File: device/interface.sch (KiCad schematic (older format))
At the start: 30 parts, among them IC1 ATTINY2313-S, J1 Screw_Terminal_1x02, J2 Screw_Terminal_01x02, P1 CONN_01X06, P2 CONN_02X03, P3 CONN_01X04, U1 L7805, U2 MAX483E, Y1 16MHz

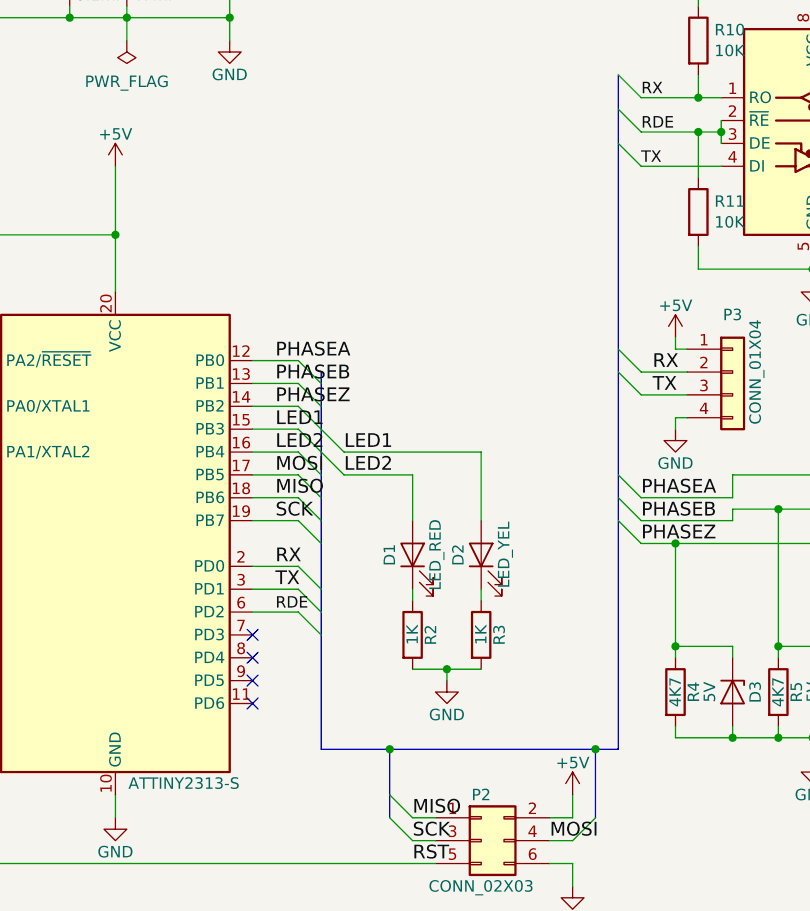
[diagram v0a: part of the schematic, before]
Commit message: added address switch
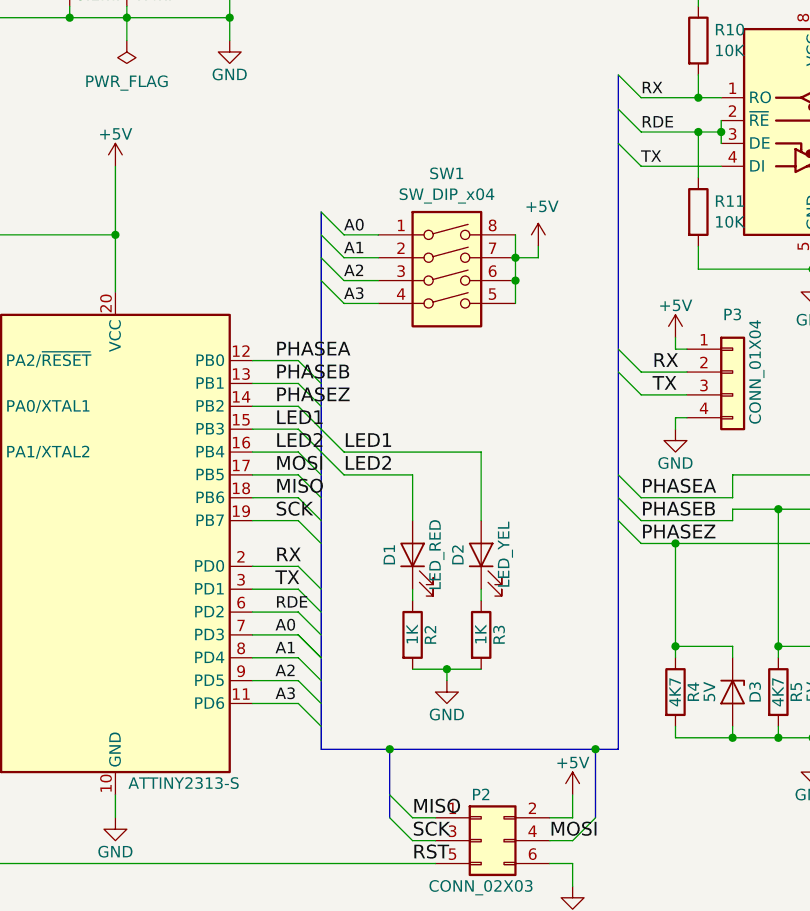
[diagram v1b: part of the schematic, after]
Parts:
- added SW1: SW_DIP_x04, Button_Switch_THT:SW_DIP_SPSTx04_Slide_9.78x12.34mm_W7.62mm_P2.54mm, symbol Switch:SW_DIP_x04
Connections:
- net +5V: now also SW1.5, SW1.6, SW1.7, SW1.8
- net A3: now reaches IC1.11 (PD6)
- net A3: now also SW1.4
- net A0: now reaches IC1.7 (PD3)
- net A0: now also SW1.1
- net A1: now reaches IC1.8 (PD4)
- net A1: now also SW1.2
- net A2: now reaches IC1.9 (PD5)
- net A2: now also SW1.3
- no-connect marks 4 -> 0
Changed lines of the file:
@@
 EESchema Schematic File Version 4
+LIBS:interface-cache
 EELAYER 26 0
 EELAYER END
@@
 	1    0    0    -1
 $EndComp
-NoConn ~ 6950 4100
-NoConn ~ 6950 4200
-NoConn ~ 6950 4300
-NoConn ~ 6950 4400
 $Comp
 L power:PWR_FLAG #FLG014
@@
 Wire Wire Line
 	9800 2050 10000 2050
+$Comp
+L Switch:SW_DIP_x04 SW1
+U 1 1 5D7BE9E3
+P 7800 2550
+F 0 "SW1" H 7800 3017 50  0000 C CNN
+F 1 "SW_DIP_x04" H 7800 2926 50  0000 C CNN
+F 2 "Button_Switch_THT:SW_DIP_SPSTx04_Slide_9.78x12.34mm_W7.62mm_P2.54mm" H 7800 2550 50  0001 C CNN
+F 3 "" H 7800 2550 50  0001 C CNN
+	1    7800 2550
+	1    0    0    -1
+$EndComp
+Wire Wire Line
+	8100 2350 8100 2450
+Wire Wire Line
+	8100 2550 8100 2450
+Connection ~ 8100 2450
+Wire Wire Line
+	8100 2650 8100 2550
+Connection ~ 8100 2550
+$Comp
+L power:+5V #PWR0103
+U 1 1 5D7CF99B
+P 8200 2400
+F 0 "#PWR0103" H 8200 2250 50  0001 C CNN
+F 1 "+5V" H 8215 2573 50  0000 C CNN
+F 2 "" H 8200 2400 50  0001 C CNN
+F 3 "" H 8200 2400 50  0001 C CNN
+	1    8200 2400
+	1    0    0    -1
+$EndComp
+Wire Wire Line
+	8200 2400 8200 2450
+Wire Wire Line
+	8200 2450 8100 2450
+Entry Wire Line
+	7250 2250 7350 2350
+Entry Wire Line
+	7250 2350 7350 2450
+Entry Wire Line
+	7250 2450 7350 2550
+Entry Wire Line
+	7250 2550 7350 2650
+Wire Wire Line
+	7500 2350 7350 2350
+Wire Wire Line
+	7500 2450 7350 2450
+Wire Wire Line
+	7500 2550 7350 2550
+Wire Wire Line
+	7500 2650 7350 2650
+Text Label 7350 2350 0    50   ~ 0
+A0
+Text Label 7350 2450 0    50   ~ 0
+A1
+Text Label 7350 2550 0    50   ~ 0
+A2
+Text Label 7350 2650 0    50   ~ 0
+A3
+Entry Wire Line
+	7150 4100 7250 4200
+Entry Wire Line
+	7150 4200 7250 4300
+Entry Wire Line
+	7150 4300 7250 4400
+Entry Wire Line
+	7150 4400 7250 4500
+Entry Wire Line
+	7150 4100 7250 4200
+Wire Wire Line
+	7150 4100 6950 4100
+Wire Wire Line
+	7150 4200 6950 4200
+Wire Wire Line
+	7150 4300 6950 4300
+Wire Wire Line
+	7150 4400 6950 4400
 Wire Bus Line
 	7550 4600 7550 4900
@@
 	8550 1650 8550 4600
 Wire Bus Line
-	7250 2950 7250 4600
+	7250 2250 7250 4600
+Text Label 7050 4100 0    50   ~ 0
+A0
+Text Label 7050 4200 0    50   ~ 0
+A1
+Text Label 7050 4300 0    50   ~ 0
+A2
+Text Label 7050 4400 0    50   ~ 0
+A3
 $EndSCHEMATC

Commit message: added address switch
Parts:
- SW1: value SW_DIP_x04 -> ADDRESS_SW
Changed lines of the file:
@@
 P 7800 2550
 F 0 "SW1" H 7800 3017 50  0000 C CNN
-F 1 "SW_DIP_x04" H 7800 2926 50  0000 C CNN
+F 1 "ADDRESS_SW" H 7800 2926 50  0000 C CNN
 F 2 "Button_Switch_THT:SW_DIP_SPSTx04_Slide_9.78x12.34mm_W7.62mm_P2.54mm" H 7800 2550 50  0001 C CNN
 F 3 "" H 7800 2550 50  0001 C CNN

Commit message: pcb update
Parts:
- added C5: 470mF, Capacitor_SMD:C_Elec_6.3x7.7, symbol Device:CP
- added C6: 0,1mF, Capacitor_SMD:C_0805_2012Metric, symbol Device:C
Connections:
- net +5V: now also C5.1, C6.1
- net GND: now also C5.2, C6.2
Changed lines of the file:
@@
 L power:+5V #PWR06
 U 1 1 5D7AEF69
-P 7300 950
-F 0 "#PWR06" H 7300 800 50  0001 C CNN
-F 1 "+5V" H 7300 1090 50  0000 C CNN
-F 2 "" H 7300 950 50  0000 C CNN
-F 3 "" H 7300 950 50  0000 C CNN
-	1    7300 950
+P 7750 950
+F 0 "#PWR06" H 7750 800 50  0001 C CNN
+F 1 "+5V" H 7750 1090 50  0000 C CNN
+F 2 "" H 7750 950 50  0000 C CNN
+F 3 "" H 7750 950 50  0000 C CNN
+	1    7750 950
 	1    0    0    -1
 $EndComp
@@
 Connection ~ 6150 1400
 Wire Wire Line
-	7300 1000 7300 950
+	7750 1000 7750 950
 Wire Bus Line
 	8450 4600 8450 4900
@@
 	6400 1000 6550 1000
 Wire Wire Line
-	7150 1000 7300 1000
+	7150 1000 7250 1000
 Wire Wire Line
 	6350 4800 6350 4900
@@
 Wire Wire Line
 	7150 4400 6950 4400
-Wire Bus Line
-	7550 4600 7550 4900
-Wire Bus Line
-	8550 1650 8550 4600
-Wire Bus Line
-	7250 2250 7250 4600
 Text Label 7050 4100 0    50   ~ 0
 A0
@@
 Text Label 7050 4400 0    50   ~ 0
 A3
+$Comp
+L Device:CP C5
+U 1 1 5D7F3934
+P 7250 1200
+F 0 "C5" H 7300 1300 50  0000 L CNN
+F 1 "470mF" H 7250 1100 50  0000 L CNN
+F 2 "Capacitor_SMD:C_Elec_6.3x7.7" H 7288 1050 50  0001 C CNN
+F 3 "~" H 7250 1200 50  0001 C CNN
+	1    7250 1200
+	1    0    0    -1
+$EndComp
+$Comp
+L Device:C C6
+U 1 1 5D7F3A01
+P 7550 1200
+F 0 "C6" H 7600 1300 50  0000 L CNN
+F 1 "0,1mF" H 7600 1100 50  0000 L CNN
+F 2 "Capacitor_SMD:C_0805_2012Metric" H 7588 1050 50  0001 C CNN
+F 3 "~" H 7550 1200 50  0001 C CNN
+	1    7550 1200
+	1    0    0    -1
+$EndComp
+Wire Wire Line
+	7250 1050 7250 1000
+Connection ~ 7250 1000
+Wire Wire Line
+	7250 1000 7550 1000
+Wire Wire Line
+	7550 1050 7550 1000
+Connection ~ 7550 1000
+Wire Wire Line
+	7550 1000 7750 1000
+Wire Wire Line
+	7250 1350 7250 1400
+Wire Wire Line
+	7250 1400 6850 1400
+Wire Wire Line
+	7550 1350 7550 1400
+Wire Wire Line
+	7550 1400 7250 1400
+Wire Bus Line
+	7550 4600 7550 4900
+Wire Bus Line
+	8550 1650 8550 4600
+Wire Bus Line
+	7250 2250 7250 4600
+Connection ~ 7250 1400
 $EndSCHEMATC

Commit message: uart pull uo
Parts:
- added R12: 10K, Resistor_SMD:R_0805_2012Metric, symbol Device:R
- C4: value 47mF -> 100mF
- C5: value 470mF -> 100mF
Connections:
- net +5V: now also R12.2
- net RX: now also R12.1
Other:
- moved on the sheet: P3
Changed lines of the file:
@@
 P 6400 1200
 F 0 "C4" H 6425 1300 50  0000 L CNN
-F 1 "47mF" H 6425 1100 50  0000 L CNN
+F 1 "100mF" H 6425 1100 50  0000 L CNN
 F 2 "Capacitor_SMD:CP_Elec_6.3x5.3" H 6438 1050 50  0001 C CNN
 F 3 "" H 6400 1200 50  0000 C CNN
@@
 L Connector_Generic:Conn_01x04 P3
 U 1 1 5D7B1EFF
-P 9050 2950
-F 0 "P3" H 9050 3200 50  0000 C CNN
-F 1 "CONN_01X04" V 9150 2950 50  0000 C CNN
-F 2 "Connector_JST:JST_XH_S4B-XH-A_1x04_P2.50mm_Horizontal" H 9050 2950 50  0001 C CNN
-F 3 "" H 9050 2950 50  0000 C CNN
-	1    9050 2950
+P 10600 2950
+F 0 "P3" H 10600 3200 50  0000 C CNN
+F 1 "CONN_01X04" V 10700 2950 50  0000 C CNN
+F 2 "Connector_JST:JST_XH_S4B-XH-A_1x04_P2.50mm_Horizontal" H 10600 2950 50  0001 C CNN
+F 3 "" H 10600 2950 50  0000 C CNN
+	1    10600 2950
 	1    0    0    -1
 $EndComp
@@
 	8800 2800 8800 2850
 Wire Wire Line
-	8800 2850 8850 2850
-Wire Wire Line
-	8850 3150 8800 3150
+	8800 2850 10200 2850
+Wire Wire Line
+	10400 3150 8800 3150
 Wire Wire Line
 	8800 3150 8800 3200
 Wire Wire Line
-	8650 3050 8850 3050
-Wire Wire Line
-	8850 2950 8650 2950
+	8650 3050 10400 3050
+Wire Wire Line
+	10400 2950 10100 2950
 Connection ~ 8800 3700
 Wire Wire Line
@@
 P 7250 1200
 F 0 "C5" H 7300 1300 50  0000 L CNN
-F 1 "470mF" H 7250 1100 50  0000 L CNN
+F 1 "100mF" H 7250 1100 50  0000 L CNN
 F 2 "Capacitor_SMD:C_Elec_6.3x7.7" H 7288 1050 50  0001 C CNN
 F 3 "~" H 7250 1200 50  0001 C CNN
@@
 Wire Wire Line
 	7550 1400 7250 1400
+Connection ~ 7250 1400
+$Comp
+L Device:R R12
+U 1 1 5D81B686
+P 10200 2600
+F 0 "R12" H 10270 2646 50  0000 L CNN
+F 1 "10K" H 10270 2555 50  0000 L CNN
+F 2 "Resistor_SMD:R_0805_2012Metric" V 10130 2600 50  0001 C CNN
+F 3 "~" H 10200 2600 50  0001 C CNN
+	1    10200 2600
+	1    0    0    -1
+$EndComp
+Wire Wire Line
+	10200 2450 10100 2450
+Wire Wire Line
+	10100 2450 10100 2950
+Connection ~ 10100 2950
+Wire Wire Line
+	10100 2950 8650 2950
+Wire Wire Line
+	10200 2750 10200 2850
 Wire Bus Line
 	7550 4600 7550 4900
@@
 Wire Bus Line
 	7250 2250 7250 4600
-Connection ~ 7250 1400
+Connection ~ 10200 2850
+Wire Wire Line
+	10200 2850 10400 2850
 $EndSCHEMATC
